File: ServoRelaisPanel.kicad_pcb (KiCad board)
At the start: 2 copper layers, 77.5 x 99.9 mm, 160 parts, among them J1 Conn_01x03_Female, J2 ISCP, J3 Conn_01x02_Female, J4 Conn_01x03_Female, U1 L78L05_SOT89, U2 PIC10F320-IP, U3 ASSR-1611

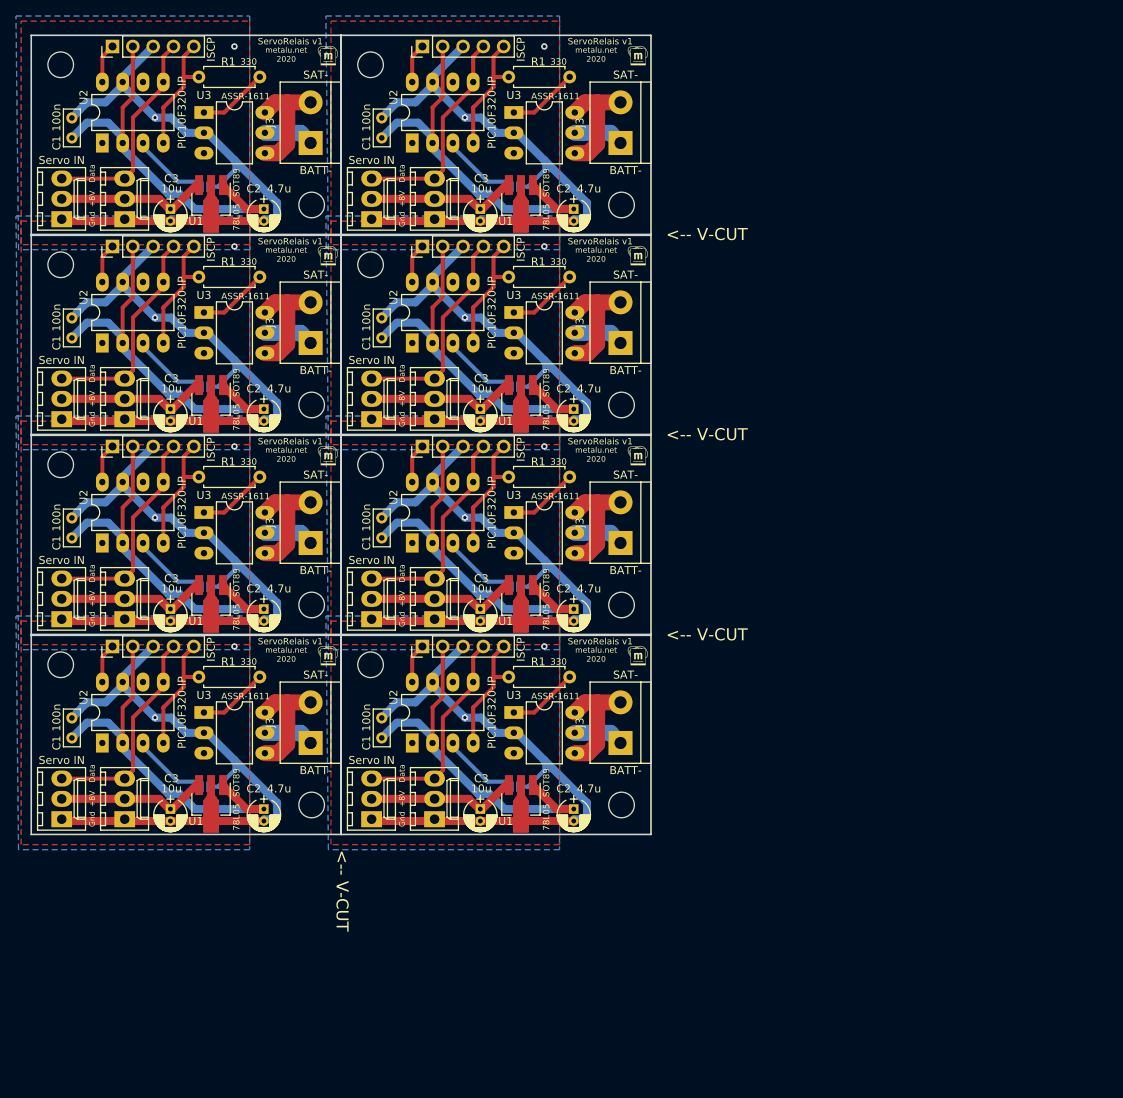
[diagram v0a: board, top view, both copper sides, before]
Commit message: finish PCB, using ASSR-1611 as a 5A circuit breaker.
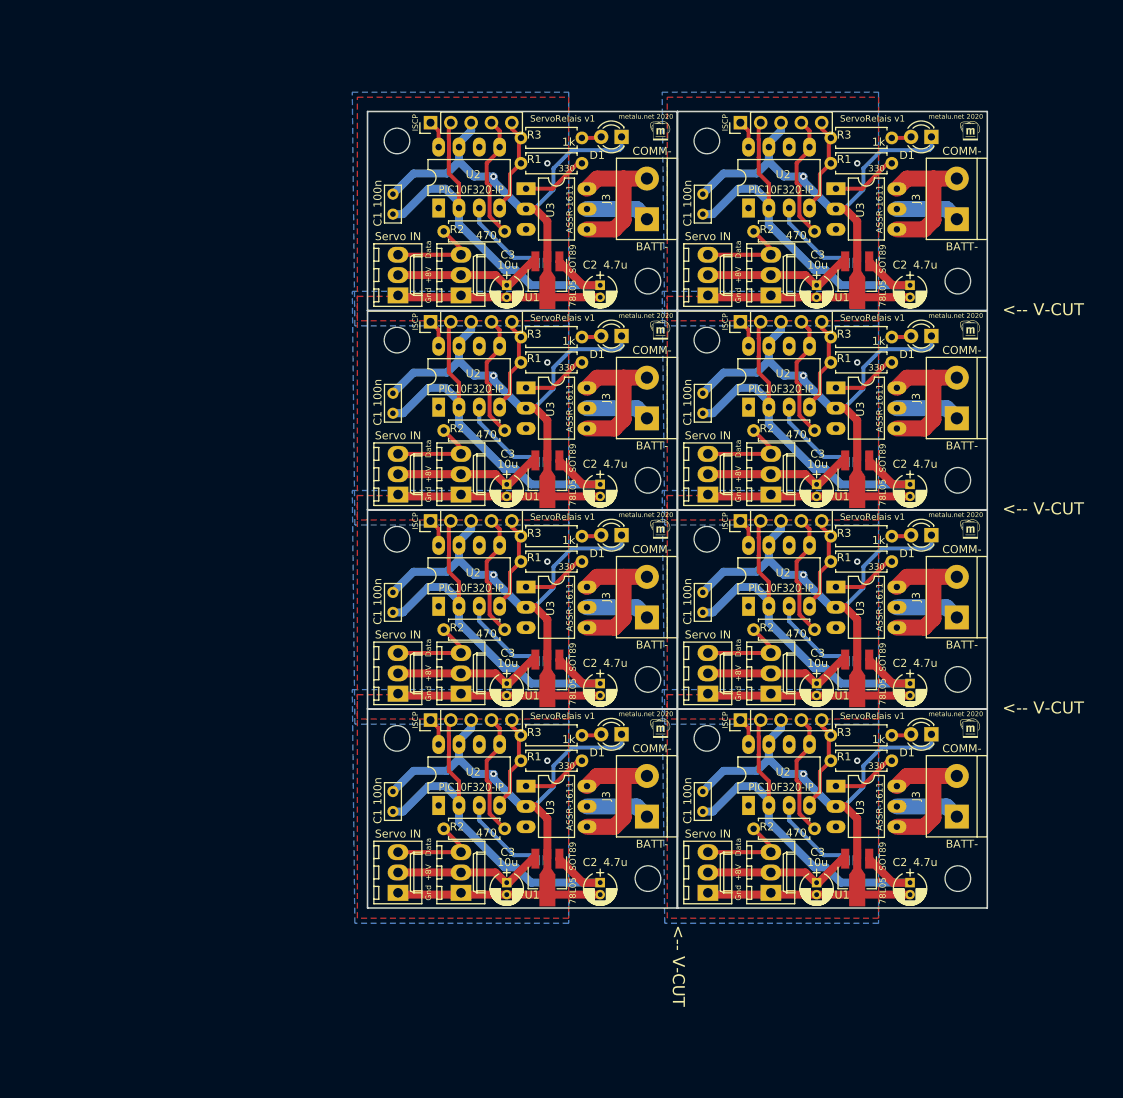
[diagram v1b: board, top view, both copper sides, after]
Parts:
- removed the ? at (110.0, 97.0)
- removed the ? at (71.2, 97.0)
- removed the ? at (110.0, 72.0)
- removed the ? at (71.2, 72.0)
- removed the ? at (110.0, 47.0)
- removed the ? at (108.7, 122.0)
- removed the ? at (70.0, 122.0)
- removed the ? at (108.7, 97.0)
- removed the ? at (70.0, 97.0)
- removed the ? at (108.7, 72.0)
- removed the ? at (70.0, 72.0)
- removed the ? at (108.7, 47.0)
- removed the ? at (108.7, 123.3)
- removed the ? at (70.0, 123.3)
- removed the ? at (108.7, 98.3)
- removed the ? at (70.0, 98.3)
- removed the ? at (108.7, 73.3)
- removed the ? at (70.0, 73.3)
- removed the ? at (108.7, 48.3)
- removed the ? at (71.2, 58.4)
- removed the ? at (110.0, 108.4)
- removed the ? at (70.0, 47.0)
- removed the ? at (71.2, 47.0)
- removed the ? at (70.0, 48.3)
- removed the ? at (71.2, 108.4)
- removed the ? at (110.0, 83.4)
- removed the ? at (71.2, 83.4)
- removed the ? at (110.0, 58.4)
- removed the ? at (110.0, 122.0)
- removed the ? at (71.2, 122.0)
- removed the C1 at (100.5, 118.2)
- removed the C1 at (61.7, 118.2)
- removed the C1 at (100.5, 93.2)
- removed the C1 at (61.7, 93.2)
- removed the C1 at (100.5, 68.2)
- removed the C1 at (61.7, 68.2)
- removed the C1 at (100.5, 43.2)
- removed the C2 at (124.5, 127.1)
- removed the C2 at (85.7, 127.1)
- removed the C2 at (124.5, 102.1)
- removed the C2 at (85.7, 102.1)
- removed the C2 at (124.5, 77.1)
- removed the C2 at (85.7, 77.1)
- removed the C2 at (124.5, 52.1)
- removed the C3 at (112.8, 127.1)
- removed the C3 at (74.0, 127.1)
- removed the C3 at (112.8, 102.1)
- removed the C3 at (74.0, 102.1)
- removed the C3 at (112.8, 77.1)
- removed the C3 at (74.0, 77.1)
- removed the C3 at (112.8, 52.1)
- removed the G*** at (128.4, 107.8)
- removed the G*** at (132.5, 82.9)
- removed the G*** at (93.7, 82.9)
- removed the G*** at (132.5, 57.9)
- removed the G*** at (93.7, 57.9)
- removed the G*** at (132.5, 32.9)
- removed the G*** at (89.7, 107.8)
- removed the G*** at (128.4, 82.8)
- removed the G*** at (89.7, 82.8)
- removed the G*** at (128.4, 57.8)
- removed the G*** at (89.7, 57.8)
- removed the G*** at (128.4, 32.8)
- removed the G*** at (132.5, 107.9)
- removed the G*** at (93.7, 107.9)
- removed the H1 at (99.1, 109.0)
- removed the H1 at (60.3, 109.0)
- removed the H1 at (99.1, 84.0)
- removed the H1 at (60.3, 84.0)
- removed the H1 at (99.1, 59.0)
- removed the H1 at (60.3, 59.0)
- removed the H1 at (99.1, 34.0)
- removed the H2 at (130.4, 126.6)
- removed the H2 at (91.7, 126.6)
- removed the H2 at (130.4, 101.6)
- removed the H2 at (91.7, 101.6)
- removed the H2 at (130.4, 76.6)
- removed the H2 at (91.7, 76.6)
- removed the H2 at (130.4, 51.6)
- removed the J1 at (99.2, 128.3)
- removed the J1 at (60.5, 128.3)
- removed the J1 at (99.2, 103.3)
- removed the J1 at (60.5, 103.3)
- removed the J1 at (99.2, 78.3)
- removed the J1 at (60.5, 78.3)
- removed the J1 at (99.2, 53.3)
- removed the J2 at (105.5, 106.8)
- removed the J2 at (66.8, 106.8)
- removed the J2 at (105.5, 81.8)
- removed the J2 at (66.8, 81.8)
- removed the J2 at (105.5, 56.8)
- removed the J2 at (66.8, 56.8)
- removed the J2 at (105.5, 31.8)
- removed the J3 at (130.3, 118.8)
- removed the J3 at (91.6, 118.8)
- removed the J3 at (130.3, 93.8)
- removed the J3 at (91.6, 93.8)
- removed the J3 at (130.3, 68.8)
- removed the J3 at (91.6, 68.8)
- removed the J3 at (130.3, 43.8)
- removed the J4 at (107.1, 128.3)
- removed the J4 at (68.3, 128.3)
- removed the J4 at (107.1, 103.3)
- removed the J4 at (68.3, 103.3)
- removed the J4 at (107.1, 78.3)
- removed the J4 at (68.3, 78.3)
- removed the J4 at (107.1, 53.3)
- removed the JP1 at (117.1, 124.3)
- removed the JP1 at (78.4, 124.3)
- removed the JP1 at (117.1, 99.3)
- removed the JP1 at (78.4, 99.3)
- removed the JP1 at (117.1, 74.3)
- removed the JP1 at (78.4, 74.3)
- removed the JP1 at (117.1, 49.3)
- removed the R1 at (124.0, 110.6)
- removed the R1 at (85.2, 110.6)
- removed the R1 at (124.0, 85.6)
- removed the R1 at (85.2, 85.6)
- removed the R1 at (124.0, 60.6)
- removed the R1 at (85.2, 60.6)
- removed the R1 at (124.0, 35.6)
- removed the U1 at (117.9, 126.1)
- removed the U1 at (79.1, 126.1)
- removed the U1 at (117.9, 101.1)
- removed the U1 at (79.1, 101.1)
- removed the U1 at (117.9, 76.1)
- removed the U1 at (79.1, 76.1)
- removed the U1 at (117.9, 51.1)
- removed the U2 at (104.3, 118.8)
- removed the U2 at (65.5, 118.8)
- removed the U2 at (104.3, 93.8)
- removed the U2 at (65.5, 93.8)
- removed the U2 at (104.3, 68.8)
- removed the U2 at (65.5, 68.8)
- removed the U2 at (104.3, 43.8)
- removed the U3 at (117.0, 115.0)
- removed the U3 at (78.2, 115.0)
- removed the U3 at (117.0, 90.0)
- removed the U3 at (78.2, 90.0)
- removed the U3 at (117.0, 65.0)
- removed the U3 at (78.2, 65.0)
- removed the U3 at (117.0, 40.0)
- added ?: , , F.Cu at (152.0, 131.2)
- added ?: , , F.Cu at (150.7, 107.6)
- added ?: , , F.Cu at (112.0, 107.6)
- added ?: , , F.Cu at (150.7, 82.7)
- added ?: , , F.Cu at (112.0, 82.7)
- added ?: , , F.Cu at (150.7, 57.8)
- added ? (x3): , , F.Cu at (152.0, 142.6)
- added ? (x2): , , F.Cu at (113.3, 142.6)
- added ?: , , F.Cu at (152.0, 117.7)
- added ?: , , F.Cu at (113.3, 117.7)
- added ?: , , F.Cu at (152.0, 92.8)
- added ?: , , F.Cu at (113.3, 131.2)
- added ?: , , F.Cu at (113.3, 92.8)
- added ?: , , F.Cu at (152.0, 67.9)
- added ?: , , F.Cu at (150.7, 131.2)
- added ?: , , F.Cu at (112.0, 131.2)
- added ?: , , F.Cu at (150.7, 106.3)
- added ?: , , F.Cu at (112.0, 106.3)
- added ?: , , F.Cu at (150.7, 81.4)
- added ?: , , F.Cu at (112.0, 81.4)
- added ?: , , F.Cu at (150.7, 56.5)
- added ?: , , F.Cu at (152.0, 106.3)
- added ?: , , F.Cu at (113.3, 67.9)
- added ?: , , F.Cu at (112.0, 56.5)
- added ?: , , F.Cu at (113.3, 56.5)
- added ?: , , F.Cu at (112.0, 57.8)
- added ?: , , F.Cu at (113.3, 106.3)
- added ?: , , F.Cu at (152.0, 81.4)
- added ?: , , F.Cu at (113.3, 81.4)
- added ?: , , F.Cu at (152.0, 56.5)
- added ?: , , F.Cu at (150.7, 132.5)
- added ?: , , F.Cu at (112.0, 132.5)
- added C1: 100n, Capacitors_ThroughHole:C_Rect_L4.6mm_W2.0mm_P2.50mm_MKS02_FKP02, F.Cu at (140.6, 127.4)
- added C1: 100n, Capacitors_ThroughHole:C_Rect_L4.6mm_W2.0mm_P2.50mm_MKS02_FKP02, F.Cu at (101.9, 127.4)
- added C1: 100n, Capacitors_ThroughHole:C_Rect_L4.6mm_W2.0mm_P2.50mm_MKS02_FKP02, F.Cu at (140.6, 102.5)
- added C1: 100n, Capacitors_ThroughHole:C_Rect_L4.6mm_W2.0mm_P2.50mm_MKS02_FKP02, F.Cu at (101.9, 102.5)
- added C1: 100n, Capacitors_ThroughHole:C_Rect_L4.6mm_W2.0mm_P2.50mm_MKS02_FKP02, F.Cu at (140.6, 77.6)
- added C1: 100n, Capacitors_ThroughHole:C_Rect_L4.6mm_W2.0mm_P2.50mm_MKS02_FKP02, F.Cu at (101.9, 77.6)
- added C1: 100n, Capacitors_ThroughHole:C_Rect_L4.6mm_W2.0mm_P2.50mm_MKS02_FKP02, F.Cu at (140.6, 52.7)
- added C2: 4.7u, Capacitors_ThroughHole:CP_Radial_D4.0mm_P1.50mm, F.Cu at (166.5, 136.3)
- added C2: 4.7u, Capacitors_ThroughHole:CP_Radial_D4.0mm_P1.50mm, F.Cu at (127.8, 136.3)
- added C2: 4.7u, Capacitors_ThroughHole:CP_Radial_D4.0mm_P1.50mm, F.Cu at (166.5, 111.4)
- added C2: 4.7u, Capacitors_ThroughHole:CP_Radial_D4.0mm_P1.50mm, F.Cu at (127.8, 111.4)
- added C2: 4.7u, Capacitors_ThroughHole:CP_Radial_D4.0mm_P1.50mm, F.Cu at (166.5, 86.5)
- added C2: 4.7u, Capacitors_ThroughHole:CP_Radial_D4.0mm_P1.50mm, F.Cu at (127.8, 86.5)
- added C2: 4.7u, Capacitors_ThroughHole:CP_Radial_D4.0mm_P1.50mm, F.Cu at (166.5, 61.6)
- added C3: 10u, Capacitors_ThroughHole:CP_Radial_D4.0mm_P1.50mm, F.Cu at (154.8, 136.3)
- added C3: 10u, Capacitors_ThroughHole:CP_Radial_D4.0mm_P1.50mm, F.Cu at (116.1, 136.3)
- added C3: 10u, Capacitors_ThroughHole:CP_Radial_D4.0mm_P1.50mm, F.Cu at (154.8, 111.4)
- added C3: 10u, Capacitors_ThroughHole:CP_Radial_D4.0mm_P1.50mm, F.Cu at (116.1, 111.4)
- added C3: 10u, Capacitors_ThroughHole:CP_Radial_D4.0mm_P1.50mm, F.Cu at (154.8, 86.5)
- added C3: 10u, Capacitors_ThroughHole:CP_Radial_D4.0mm_P1.50mm, F.Cu at (116.1, 86.5)
- added C3: 10u, Capacitors_ThroughHole:CP_Radial_D4.0mm_P1.50mm, F.Cu at (154.8, 61.6)
- added D1: LED, LEDs:LED_D3.0mm, F.Cu at (169.2, 117.7)
- added D1: LED, LEDs:LED_D3.0mm, F.Cu at (130.4, 117.7)
- added D1: LED, LEDs:LED_D3.0mm, F.Cu at (169.2, 92.8)
- added D1: LED, LEDs:LED_D3.0mm, F.Cu at (130.4, 92.8)
- added D1: LED, LEDs:LED_D3.0mm, F.Cu at (169.2, 67.9)
- added D1: LED, LEDs:LED_D3.0mm, F.Cu at (130.4, 67.9)
- added D1: LED, LEDs:LED_D3.0mm, F.Cu at (169.2, 43.1)
- added D1: LED, LEDs:LED_D3.0mm, F.Cu at (130.4, 43.1)
- added G***: LOGO, metalunet:metalunet, B.Cu at (166.9, 132.3)
- added G***: LOGO, metalunet:metalunet-mini, F.Cu at (174.0, 92.1)
- added G***: LOGO, metalunet:metalunet-mini, F.Cu at (135.3, 92.1)
- added G***: LOGO, metalunet:metalunet-mini, F.Cu at (174.0, 67.2)
- added G***: LOGO, metalunet:metalunet-mini, F.Cu at (135.3, 67.2)
- added G***: LOGO, metalunet:metalunet-mini, F.Cu at (174.0, 42.3)
- added G***: LOGO, metalunet:metalunet, B.Cu at (128.1, 132.3)
- added G***: LOGO, metalunet:metalunet, B.Cu at (166.9, 107.4)
- added G***: LOGO, metalunet:metalunet, B.Cu at (128.1, 107.4)
- added G***: LOGO, metalunet:metalunet, B.Cu at (166.9, 82.5)
- added G***: LOGO, metalunet:metalunet, B.Cu at (128.1, 82.5)
- added G***: LOGO, metalunet:metalunet, B.Cu at (166.9, 57.7)
- added G***: LOGO, metalunet:metalunet-mini, F.Cu at (174.0, 117.0)
- added G***: LOGO, metalunet:metalunet-mini, F.Cu at (135.3, 117.0)
- added H1: MountingHole, Mounting_Holes:MountingHole_3.2mm_M3, F.Cu at (141.1, 118.2)
- added H1: MountingHole, Mounting_Holes:MountingHole_3.2mm_M3, F.Cu at (102.4, 118.2)
- added H1: MountingHole, Mounting_Holes:MountingHole_3.2mm_M3, F.Cu at (141.1, 93.3)
- added H1: MountingHole, Mounting_Holes:MountingHole_3.2mm_M3, F.Cu at (102.4, 93.3)
- added H1: MountingHole, Mounting_Holes:MountingHole_3.2mm_M3, F.Cu at (141.1, 68.5)
- added H1: MountingHole, Mounting_Holes:MountingHole_3.2mm_M3, F.Cu at (102.4, 68.5)
- added H1: MountingHole, Mounting_Holes:MountingHole_3.2mm_M3, F.Cu at (141.1, 43.6)
- added H2: MountingHole, Mounting_Holes:MountingHole_3.2mm_M3, F.Cu at (172.5, 135.8)
- added H2: MountingHole, Mounting_Holes:MountingHole_3.2mm_M3, F.Cu at (133.7, 135.8)
- added H2: MountingHole, Mounting_Holes:MountingHole_3.2mm_M3, F.Cu at (172.5, 110.9)
- added H2: MountingHole, Mounting_Holes:MountingHole_3.2mm_M3, F.Cu at (133.7, 110.9)
- added H2: MountingHole, Mounting_Holes:MountingHole_3.2mm_M3, F.Cu at (172.5, 86.0)
- added H2: MountingHole, Mounting_Holes:MountingHole_3.2mm_M3, F.Cu at (133.7, 86.0)
- added H2: MountingHole, Mounting_Holes:MountingHole_3.2mm_M3, F.Cu at (172.5, 61.1)
- added J1: Conn_01x03_Female, Connectors_Molex:Molex_KK-6410-03_03x2.54mm_Straight, F.Cu at (141.2, 137.5)
- added J1: Conn_01x03_Female, Connectors_Molex:Molex_KK-6410-03_03x2.54mm_Straight, F.Cu at (102.5, 137.5)
- added J1: Conn_01x03_Female, Connectors_Molex:Molex_KK-6410-03_03x2.54mm_Straight, F.Cu at (141.2, 112.6)
- added J1: Conn_01x03_Female, Connectors_Molex:Molex_KK-6410-03_03x2.54mm_Straight, F.Cu at (102.5, 112.6)
- added J1: Conn_01x03_Female, Connectors_Molex:Molex_KK-6410-03_03x2.54mm_Straight, F.Cu at (141.2, 87.8)
- added J1: Conn_01x03_Female, Connectors_Molex:Molex_KK-6410-03_03x2.54mm_Straight, F.Cu at (102.5, 87.8)
- added J1: Conn_01x03_Female, Connectors_Molex:Molex_KK-6410-03_03x2.54mm_Straight, F.Cu at (141.2, 62.9)
- added J2: ISCP, Pin_Headers:Pin_Header_Straight_1x05_Pitch2.54mm, F.Cu at (145.3, 116.0)
- added J2: ISCP, Pin_Headers:Pin_Header_Straight_1x05_Pitch2.54mm, F.Cu at (106.6, 116.0)
- added J2: ISCP, Pin_Headers:Pin_Header_Straight_1x05_Pitch2.54mm, F.Cu at (145.3, 91.1)
- added J2: ISCP, Pin_Headers:Pin_Header_Straight_1x05_Pitch2.54mm, F.Cu at (106.6, 91.1)
- added J2: ISCP, Pin_Headers:Pin_Header_Straight_1x05_Pitch2.54mm, F.Cu at (145.3, 66.2)
- added J2: ISCP, Pin_Headers:Pin_Header_Straight_1x05_Pitch2.54mm, F.Cu at (106.6, 66.2)
- added J2: ISCP, Pin_Headers:Pin_Header_Straight_1x05_Pitch2.54mm, F.Cu at (145.3, 41.3)
- added J3: Conn_01x02_Female, Terminal_Blocks:TerminalBlock_bornier-2_P5.08mm, F.Cu at (172.3, 128.0)
- added J3: Conn_01x02_Female, Terminal_Blocks:TerminalBlock_bornier-2_P5.08mm, F.Cu at (133.6, 128.0)
- added J3: Conn_01x02_Female, Terminal_Blocks:TerminalBlock_bornier-2_P5.08mm, F.Cu at (172.3, 103.1)
- added J3: Conn_01x02_Female, Terminal_Blocks:TerminalBlock_bornier-2_P5.08mm, F.Cu at (133.6, 103.1)
- added J3: Conn_01x02_Female, Terminal_Blocks:TerminalBlock_bornier-2_P5.08mm, F.Cu at (172.3, 78.2)
- added J3: Conn_01x02_Female, Terminal_Blocks:TerminalBlock_bornier-2_P5.08mm, F.Cu at (133.6, 78.2)
- added J3: Conn_01x02_Female, Terminal_Blocks:TerminalBlock_bornier-2_P5.08mm, F.Cu at (172.3, 53.3)
- added J4: Conn_01x03_Female, Connectors_Molex:Molex_KK-6410-03_03x2.54mm_Straight, F.Cu at (149.1, 137.5)
- added J4: Conn_01x03_Female, Connectors_Molex:Molex_KK-6410-03_03x2.54mm_Straight, F.Cu at (110.4, 137.5)
- added J4: Conn_01x03_Female, Connectors_Molex:Molex_KK-6410-03_03x2.54mm_Straight, F.Cu at (149.1, 112.6)
- added J4: Conn_01x03_Female, Connectors_Molex:Molex_KK-6410-03_03x2.54mm_Straight, F.Cu at (110.4, 112.6)
- added J4: Conn_01x03_Female, Connectors_Molex:Molex_KK-6410-03_03x2.54mm_Straight, F.Cu at (149.1, 87.8)
- added J4: Conn_01x03_Female, Connectors_Molex:Molex_KK-6410-03_03x2.54mm_Straight, F.Cu at (110.4, 87.8)
- added J4: Conn_01x03_Female, Connectors_Molex:Molex_KK-6410-03_03x2.54mm_Straight, F.Cu at (149.1, 62.9)
- added JP1: Config, Connect:GS2, B.Cu at (159.1, 133.5)
- added JP1: Config, Connect:GS2, B.Cu at (120.4, 133.5)
- added JP1: Config, Connect:GS2, B.Cu at (159.1, 108.6)
- added JP1: Config, Connect:GS2, B.Cu at (120.4, 108.6)
- added JP1: Config, Connect:GS2, B.Cu at (159.1, 83.7)
- added JP1: Config, Connect:GS2, B.Cu at (120.4, 83.7)
- added JP1: Config, Connect:GS2, B.Cu at (159.1, 58.8)
- added R1: 330, Resistors_ThroughHole:R_Axial_DIN0207_L6.3mm_D2.5mm_P7.62mm_Horizontal, F.Cu at (164.2, 121.0)
- added R1: 330, Resistors_ThroughHole:R_Axial_DIN0207_L6.3mm_D2.5mm_P7.62mm_Horizontal, F.Cu at (125.5, 121.0)
- added R1: 330, Resistors_ThroughHole:R_Axial_DIN0207_L6.3mm_D2.5mm_P7.62mm_Horizontal, F.Cu at (164.2, 96.1)
- added R1: 330, Resistors_ThroughHole:R_Axial_DIN0207_L6.3mm_D2.5mm_P7.62mm_Horizontal, F.Cu at (125.5, 96.1)
- added R1: 330, Resistors_ThroughHole:R_Axial_DIN0207_L6.3mm_D2.5mm_P7.62mm_Horizontal, F.Cu at (164.2, 71.2)
- added R1: 330, Resistors_ThroughHole:R_Axial_DIN0207_L6.3mm_D2.5mm_P7.62mm_Horizontal, F.Cu at (125.5, 71.2)
- added R1: 330, Resistors_ThroughHole:R_Axial_DIN0207_L6.3mm_D2.5mm_P7.62mm_Horizontal, F.Cu at (164.2, 46.4)
- added R2: 470, Resistors_ThroughHole:R_Axial_DIN0207_L6.3mm_D2.5mm_P7.62mm_Horizontal, F.Cu at (154.6, 129.5)
- added R2: 470, Resistors_ThroughHole:R_Axial_DIN0207_L6.3mm_D2.5mm_P7.62mm_Horizontal, F.Cu at (115.8, 129.5)
- added R2: 470, Resistors_ThroughHole:R_Axial_DIN0207_L6.3mm_D2.5mm_P7.62mm_Horizontal, F.Cu at (154.6, 104.6)
- added R2: 470, Resistors_ThroughHole:R_Axial_DIN0207_L6.3mm_D2.5mm_P7.62mm_Horizontal, F.Cu at (115.8, 104.6)
- added R2: 470, Resistors_ThroughHole:R_Axial_DIN0207_L6.3mm_D2.5mm_P7.62mm_Horizontal, F.Cu at (154.6, 79.8)
- added R2: 470, Resistors_ThroughHole:R_Axial_DIN0207_L6.3mm_D2.5mm_P7.62mm_Horizontal, F.Cu at (115.8, 79.8)
- added R2: 470, Resistors_ThroughHole:R_Axial_DIN0207_L6.3mm_D2.5mm_P7.62mm_Horizontal, F.Cu at (154.6, 54.9)
- added R2: 470, Resistors_ThroughHole:R_Axial_DIN0207_L6.3mm_D2.5mm_P7.62mm_Horizontal, F.Cu at (115.8, 54.9)
- added R3: 1k, Resistors_ThroughHole:R_Axial_DIN0207_L6.3mm_D2.5mm_P7.62mm_Horizontal, F.Cu at (164.2, 117.9)
- added R3: 1k, Resistors_ThroughHole:R_Axial_DIN0207_L6.3mm_D2.5mm_P7.62mm_Horizontal, F.Cu at (125.5, 117.9)
- added R3: 1k, Resistors_ThroughHole:R_Axial_DIN0207_L6.3mm_D2.5mm_P7.62mm_Horizontal, F.Cu at (164.2, 93.0)
- added R3: 1k, Resistors_ThroughHole:R_Axial_DIN0207_L6.3mm_D2.5mm_P7.62mm_Horizontal, F.Cu at (125.5, 93.0)
- added R3: 1k, Resistors_ThroughHole:R_Axial_DIN0207_L6.3mm_D2.5mm_P7.62mm_Horizontal, F.Cu at (164.2, 68.1)
- added R3: 1k, Resistors_ThroughHole:R_Axial_DIN0207_L6.3mm_D2.5mm_P7.62mm_Horizontal, F.Cu at (125.5, 68.1)
- added R3: 1k, Resistors_ThroughHole:R_Axial_DIN0207_L6.3mm_D2.5mm_P7.62mm_Horizontal, F.Cu at (164.2, 43.2)
- added R3: 1k, Resistors_ThroughHole:R_Axial_DIN0207_L6.3mm_D2.5mm_P7.62mm_Horizontal, F.Cu at (125.5, 43.2)
- added U1: L78L05_SOT89, TO_SOT_Packages_SMD:SOT-89-3_Handsoldering, F.Cu at (159.9, 135.3)
- added U1: L78L05_SOT89, TO_SOT_Packages_SMD:SOT-89-3_Handsoldering, F.Cu at (121.2, 135.3)
- added U1: L78L05_SOT89, TO_SOT_Packages_SMD:SOT-89-3_Handsoldering, F.Cu at (159.9, 110.4)
- added U1: L78L05_SOT89, TO_SOT_Packages_SMD:SOT-89-3_Handsoldering, F.Cu at (121.2, 110.4)
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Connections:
- J1 pad 3: /PGD -> Net-(J1-Pad3)
- J4 pad 3: /PGD -> Net-(J1-Pad3)
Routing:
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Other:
- board size 77.5 x 99.9 mm -> 77.5 x 99.6 mm
- board text added: "COMM-"
- board text removed: "SAT-"

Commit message: use a 3v->9V dc-dc converter. version 1.3
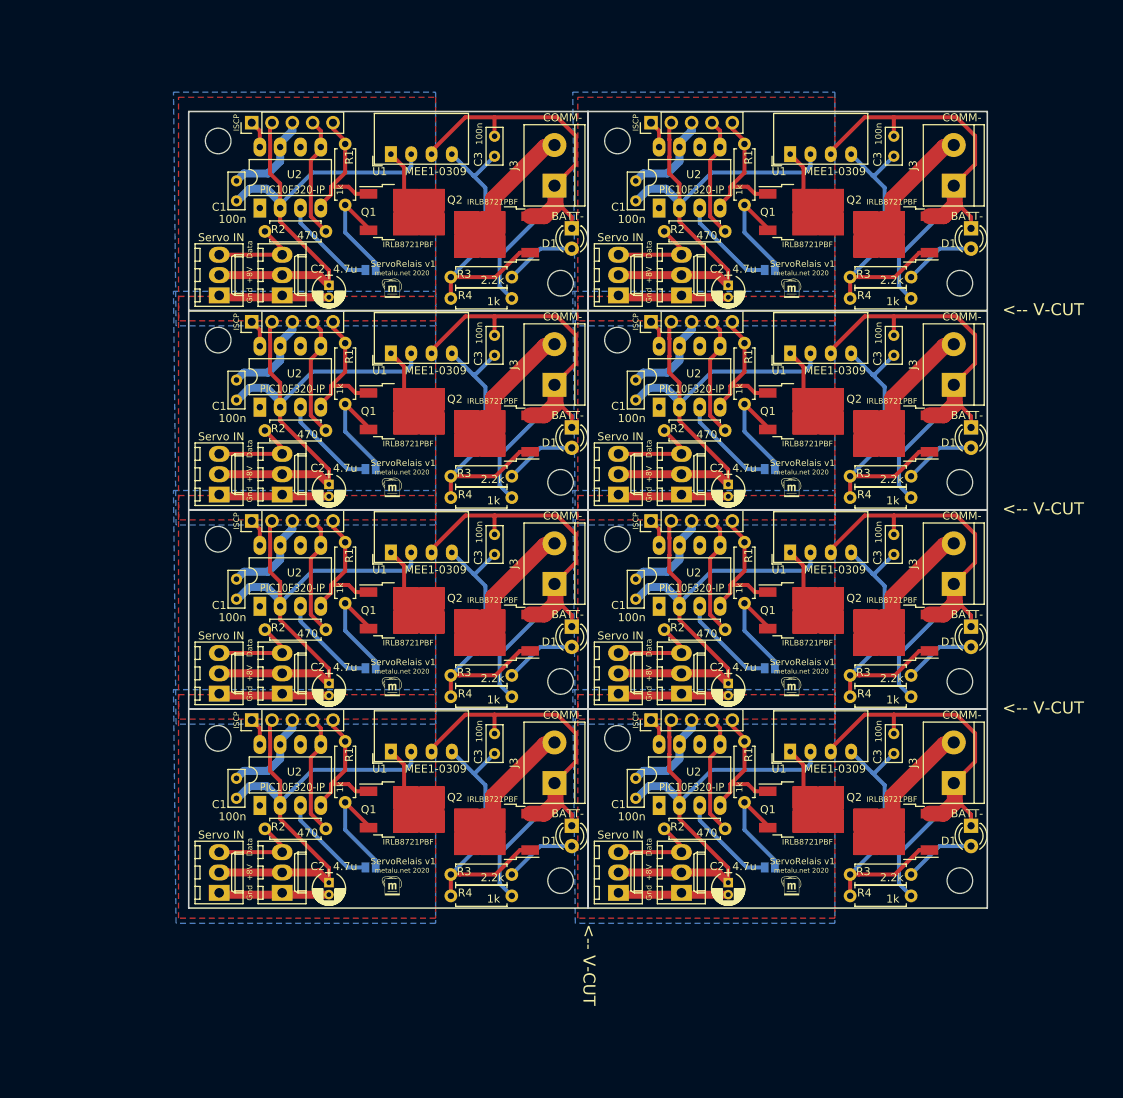
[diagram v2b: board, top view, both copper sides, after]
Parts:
- removed the ? at (152.0, 131.2)
- removed the ? at (150.7, 107.6)
- removed the ? at (112.0, 107.6)
- removed the ? at (150.7, 82.7)
- removed the ? at (112.0, 82.7)
- removed the ? at (150.7, 57.8)
- removed the ? at (152.0, 142.6) (x3)
- removed the ? at (113.3, 142.6) (x2)
- removed the ? at (152.0, 117.7)
- removed the ? at (113.3, 117.7)
- removed the ? at (152.0, 92.8)
- removed the ? at (113.3, 131.2)
- removed the ? at (113.3, 92.8)
- removed the ? at (152.0, 67.9)
- removed the ? at (150.7, 131.2)
- removed the ? at (112.0, 131.2)
- removed the ? at (150.7, 106.3)
- removed the ? at (112.0, 106.3)
- removed the ? at (150.7, 81.4)
- removed the ? at (112.0, 81.4)
- removed the ? at (150.7, 56.5)
- removed the ? at (152.0, 106.3)
- removed the ? at (113.3, 67.9)
- removed the ? at (112.0, 56.5)
- removed the ? at (113.3, 56.5)
- removed the ? at (112.0, 57.8)
- removed the ? at (113.3, 106.3)
- removed the ? at (152.0, 81.4)
- removed the ? at (113.3, 81.4)
- removed the ? at (152.0, 56.5)
- removed the ? at (150.7, 132.5)
- removed the ? at (112.0, 132.5)
- removed the C1 at (140.6, 127.4)
- removed the C1 at (101.9, 127.4)
- removed the C1 at (140.6, 102.5)
- removed the C1 at (101.9, 102.5)
- removed the C1 at (140.6, 77.6)
- removed the C1 at (101.9, 77.6)
- removed the C1 at (140.6, 52.7)
- removed the C1 at (101.9, 52.7)
- removed the C2 at (166.5, 136.3)
- removed the C2 at (127.8, 136.3)
- removed the C2 at (166.5, 111.4)
- removed the C2 at (127.8, 111.4)
- removed the C2 at (166.5, 86.5)
- removed the C2 at (127.8, 86.5)
- removed the C2 at (166.5, 61.6)
- removed the C3 at (154.8, 136.3)
- removed the C3 at (116.1, 136.3)
- removed the C3 at (154.8, 111.4)
- removed the C3 at (116.1, 111.4)
- removed the C3 at (154.8, 86.5)
- removed the C3 at (116.1, 86.5)
- removed the C3 at (154.8, 61.6)
- removed the C3 at (116.1, 61.6)
- removed the D1 at (169.2, 117.7)
- removed the D1 at (130.4, 117.7)
- removed the D1 at (169.2, 92.8)
- removed the D1 at (130.4, 92.8)
- removed the D1 at (169.2, 67.9)
- removed the D1 at (130.4, 67.9)
- removed the D1 at (169.2, 43.1)
- removed the D1 at (130.4, 43.1)
- removed the G*** at (166.9, 132.3)
- removed the G*** at (174.0, 92.1)
- removed the G*** at (135.3, 92.1)
- removed the G*** at (174.0, 67.2)
- removed the G*** at (135.3, 67.2)
- removed the G*** at (174.0, 42.3)
- removed the G*** at (128.1, 57.7)
- removed the G*** at (135.3, 42.3)
- removed the G*** at (128.1, 132.3)
- removed the G*** at (166.9, 107.4)
- removed the G*** at (128.1, 107.4)
- removed the G*** at (166.9, 82.5)
- removed the G*** at (128.1, 82.5)
- removed the G*** at (166.9, 57.7)
- removed the G*** at (174.0, 117.0)
- removed the G*** at (135.3, 117.0)
- removed the H1 at (141.1, 118.2)
- removed the H1 at (102.4, 118.2)
- removed the H1 at (141.1, 93.3)
- removed the H1 at (102.4, 93.3)
- removed the H1 at (141.1, 68.5)
- removed the H1 at (102.4, 68.5)
- removed the H1 at (141.1, 43.6)
- removed the H2 at (172.5, 135.8)
- removed the H2 at (133.7, 135.8)
- removed the H2 at (172.5, 110.9)
- removed the H2 at (133.7, 110.9)
- removed the H2 at (172.5, 86.0)
- removed the H2 at (133.7, 86.0)
- removed the H2 at (172.5, 61.1)
- removed the J1 at (141.2, 137.5)
- removed the J1 at (102.5, 137.5)
- removed the J1 at (141.2, 112.6)
- removed the J1 at (102.5, 112.6)
- removed the J1 at (141.2, 87.8)
- removed the J1 at (102.5, 87.8)
- removed the J1 at (141.2, 62.9)
- removed the J2 at (145.3, 116.0)
- removed the J2 at (106.6, 116.0)
- removed the J2 at (145.3, 91.1)
- removed the J2 at (106.6, 91.1)
- removed the J2 at (145.3, 66.2)
- removed the J2 at (106.6, 66.2)
- removed the J2 at (145.3, 41.3)
- removed the J3 at (172.3, 128.0)
- removed the J3 at (133.6, 128.0)
- removed the J3 at (172.3, 103.1)
- removed the J3 at (133.6, 103.1)
- removed the J3 at (172.3, 78.2)
- removed the J3 at (133.6, 78.2)
- removed the J3 at (172.3, 53.3)
- removed the J4 at (149.1, 137.5)
- removed the J4 at (110.4, 137.5)
- removed the J4 at (149.1, 112.6)
- removed the J4 at (110.4, 112.6)
- removed the J4 at (149.1, 87.8)
- removed the J4 at (110.4, 87.8)
- removed the J4 at (149.1, 62.9)
- removed the JP1 at (159.1, 133.5)
- removed the JP1 at (120.4, 133.5)
- removed the JP1 at (159.1, 108.6)
- removed the JP1 at (120.4, 108.6)
- removed the JP1 at (159.1, 83.7)
- removed the JP1 at (120.4, 83.7)
- removed the JP1 at (159.1, 58.8)
- removed the R1 at (164.2, 121.0)
- removed the R1 at (125.5, 121.0)
- removed the R1 at (164.2, 96.1)
- removed the R1 at (125.5, 96.1)
- removed the R1 at (164.2, 71.2)
- removed the R1 at (125.5, 71.2)
- removed the R1 at (164.2, 46.4)
- removed the R2 at (154.6, 129.5)
- removed the R2 at (115.8, 129.5)
- removed the R2 at (154.6, 104.6)
- removed the R2 at (115.8, 104.6)
- removed the R2 at (154.6, 79.8)
- removed the R2 at (115.8, 79.8)
- removed the R2 at (154.6, 54.9)
- removed the R2 at (115.8, 54.9)
- removed the R3 at (164.2, 117.9)
- removed the R3 at (125.5, 117.9)
- removed the R3 at (164.2, 93.0)
- removed the R3 at (125.5, 93.0)
- removed the R3 at (164.2, 68.1)
- removed the R3 at (125.5, 68.1)
- removed the R3 at (164.2, 43.2)
- removed the U1 at (159.9, 135.3)
- removed the U1 at (121.2, 135.3)
- removed the U1 at (159.9, 110.4)
- removed the U1 at (121.2, 110.4)
- removed the U1 at (159.9, 85.5)
- removed the U1 at (121.2, 85.5)
- removed the U1 at (159.9, 60.6)
- removed the U1 at (121.2, 60.6)
- removed the U2 at (146.3, 126.6)
- removed the U2 at (107.6, 126.6)
- removed the U2 at (146.3, 101.7)
- removed the U2 at (107.6, 101.7)
- removed the U2 at (146.3, 76.8)
- removed the U2 at (107.6, 76.8)
- removed the U2 at (146.3, 51.9)
- removed the U2 at (107.6, 51.9)
- removed U3 (x8): ASSR-1611, Housings_DIP:DIP-6_W7.62mm_LongPads
- added ?: , , F.Cu at (140.8, 142.6)
- added ?: , , F.Cu at (140.8, 106.3)
- added ?: , , F.Cu at (90.9, 106.3)
- added ?: , , F.Cu at (140.8, 81.4)
- added ?: , , F.Cu at (90.9, 81.4)
- added ?: , , F.Cu at (140.8, 56.5)
- added ?: , , F.Cu at (139.6, 131.2)
- added ?: , , F.Cu at (89.7, 131.2)
- added ?: , , F.Cu at (139.6, 106.3)
- added ?: , , F.Cu at (89.7, 106.3)
- added ?: , , F.Cu at (139.6, 81.4)
- added ?: , , F.Cu at (90.9, 142.6)
- added ?: , , F.Cu at (89.7, 81.4)
- added ?: , , F.Cu at (139.6, 56.5)
- added ?: , , F.Cu at (139.6, 132.5)
- added ?: , , F.Cu at (89.7, 132.5)
- added ?: , , F.Cu at (139.6, 107.6)
- added ?: , , F.Cu at (89.7, 107.6)
- added ?: , , F.Cu at (139.6, 82.7)
- added ?: , , F.Cu at (89.7, 82.7)
- added ?: , , F.Cu at (139.6, 57.8)
- added ?: , , F.Cu at (140.8, 117.7)
- added ?: , , F.Cu at (90.9, 67.9)
- added ?: , , F.Cu at (89.7, 56.5)
- added ?: , , F.Cu at (90.9, 56.5)
- added ?: , , F.Cu at (89.7, 57.8)
- added ?: , , F.Cu at (90.9, 117.7)
- added ?: , , F.Cu at (140.8, 92.8)
- added ?: , , F.Cu at (90.9, 92.8)
- added ?: , , F.Cu at (140.8, 67.9)
- added ?: , , F.Cu at (140.8, 131.2)
- added ?: , , F.Cu at (90.9, 131.2)
- added C1: 100n, Capacitors_ThroughHole:C_Rect_L4.6mm_W2.0mm_P2.50mm_MKS02_FKP02, F.Cu at (132.2, 125.7)
- added C1: 100n, Capacitors_ThroughHole:C_Rect_L4.6mm_W2.0mm_P2.50mm_MKS02_FKP02, F.Cu at (82.3, 125.7)
- added C1: 100n, Capacitors_ThroughHole:C_Rect_L4.6mm_W2.0mm_P2.50mm_MKS02_FKP02, F.Cu at (132.2, 100.8)
- added C1: 100n, Capacitors_ThroughHole:C_Rect_L4.6mm_W2.0mm_P2.50mm_MKS02_FKP02, F.Cu at (82.3, 100.8)
- added C1: 100n, Capacitors_ThroughHole:C_Rect_L4.6mm_W2.0mm_P2.50mm_MKS02_FKP02, F.Cu at (132.2, 75.9)
- added C1: 100n, Capacitors_ThroughHole:C_Rect_L4.6mm_W2.0mm_P2.50mm_MKS02_FKP02, F.Cu at (82.3, 75.9)
- added C1: 100n, Capacitors_ThroughHole:C_Rect_L4.6mm_W2.0mm_P2.50mm_MKS02_FKP02, F.Cu at (132.2, 51.1)
- added C1: 100n, Capacitors_ThroughHole:C_Rect_L4.6mm_W2.0mm_P2.50mm_MKS02_FKP02, F.Cu at (82.3, 51.1)
- added C2: 4.7u, Capacitors_ThroughHole:CP_Radial_D4.0mm_P1.50mm, F.Cu at (143.8, 136.3)
- added C2: 4.7u, Capacitors_ThroughHole:CP_Radial_D4.0mm_P1.50mm, F.Cu at (93.9, 136.3)
- added C2: 4.7u, Capacitors_ThroughHole:CP_Radial_D4.0mm_P1.50mm, F.Cu at (143.8, 111.4)
- added C2: 4.7u, Capacitors_ThroughHole:CP_Radial_D4.0mm_P1.50mm, F.Cu at (93.9, 111.4)
- added C2: 4.7u, Capacitors_ThroughHole:CP_Radial_D4.0mm_P1.50mm, F.Cu at (143.8, 86.5)
- added C2: 4.7u, Capacitors_ThroughHole:CP_Radial_D4.0mm_P1.50mm, F.Cu at (93.9, 86.5)
- added C2: 4.7u, Capacitors_ThroughHole:CP_Radial_D4.0mm_P1.50mm, F.Cu at (143.8, 61.6)
- added C3: 100n, Capacitors_ThroughHole:C_Rect_L4.6mm_W2.0mm_P2.50mm_MKS02_FKP02, F.Cu at (164.5, 120.1)
- added C3: 100n, Capacitors_ThroughHole:C_Rect_L4.6mm_W2.0mm_P2.50mm_MKS02_FKP02, F.Cu at (114.6, 120.1)
- added C3: 100n, Capacitors_ThroughHole:C_Rect_L4.6mm_W2.0mm_P2.50mm_MKS02_FKP02, F.Cu at (164.5, 95.2)
- added C3: 100n, Capacitors_ThroughHole:C_Rect_L4.6mm_W2.0mm_P2.50mm_MKS02_FKP02, F.Cu at (114.6, 95.2)
- added C3: 100n, Capacitors_ThroughHole:C_Rect_L4.6mm_W2.0mm_P2.50mm_MKS02_FKP02, F.Cu at (164.5, 70.4)
- added C3: 100n, Capacitors_ThroughHole:C_Rect_L4.6mm_W2.0mm_P2.50mm_MKS02_FKP02, F.Cu at (114.6, 70.4)
- added C3: 100n, Capacitors_ThroughHole:C_Rect_L4.6mm_W2.0mm_P2.50mm_MKS02_FKP02, F.Cu at (164.5, 45.5)
- added C3: 100n, Capacitors_ThroughHole:C_Rect_L4.6mm_W2.0mm_P2.50mm_MKS02_FKP02, F.Cu at (114.6, 45.5)
- added D1: LED, LEDs:LED_D3.0mm, F.Cu at (174.1, 129.2)
- added D1: LED, LEDs:LED_D3.0mm, F.Cu at (124.2, 129.2)
- added D1: LED, LEDs:LED_D3.0mm, F.Cu at (174.1, 104.3)
- added D1: LED, LEDs:LED_D3.0mm, F.Cu at (124.2, 104.3)
- added D1: LED, LEDs:LED_D3.0mm, F.Cu at (174.1, 79.4)
- added D1: LED, LEDs:LED_D3.0mm, F.Cu at (124.2, 79.4)
- added D1: LED, LEDs:LED_D3.0mm, F.Cu at (174.1, 54.5)
- added D1: LED, LEDs:LED_D3.0mm, F.Cu at (124.2, 54.5)
- added G***: LOGO, metalunet:metalunet, B.Cu at (159.1, 127.6)
- added G***: LOGO, metalunet:metalunet-mini, F.Cu at (151.6, 111.8)
- added G***: LOGO, metalunet:metalunet-mini, F.Cu at (101.7, 111.8)
- added G***: LOGO, metalunet:metalunet-mini, F.Cu at (151.6, 86.9)
- added G***: LOGO, metalunet:metalunet-mini, F.Cu at (101.7, 86.9)
- added G***: LOGO, metalunet:metalunet-mini, F.Cu at (151.6, 62.0)
- added G***: LOGO, metalunet:metalunet, B.Cu at (109.2, 53.0)
- added G***: LOGO, metalunet:metalunet-mini, F.Cu at (101.7, 62.0)
- added G***: LOGO, metalunet:metalunet, B.Cu at (109.2, 127.6)
- added G***: LOGO, metalunet:metalunet, B.Cu at (159.1, 102.7)
- added G***: LOGO, metalunet:metalunet, B.Cu at (109.2, 102.7)
- added G***: LOGO, metalunet:metalunet, B.Cu at (159.1, 77.9)
- added G***: LOGO, metalunet:metalunet, B.Cu at (109.2, 77.9)
- added G***: LOGO, metalunet:metalunet, B.Cu at (159.1, 53.0)
- added G***: LOGO, metalunet:metalunet-mini, F.Cu at (151.6, 136.7)
- added G***: LOGO, metalunet:metalunet-mini, F.Cu at (101.7, 136.7)
- added H1: MountingHole, Mounting_Holes:MountingHole_3.2mm_M3, F.Cu at (129.9, 118.2)
- added H1: MountingHole, Mounting_Holes:MountingHole_3.2mm_M3, F.Cu at (80.0, 118.2)
- added H1: MountingHole, Mounting_Holes:MountingHole_3.2mm_M3, F.Cu at (129.9, 93.3)
- added H1: MountingHole, Mounting_Holes:MountingHole_3.2mm_M3, F.Cu at (80.0, 93.3)
- added H1: MountingHole, Mounting_Holes:MountingHole_3.2mm_M3, F.Cu at (129.9, 68.5)
- added H1: MountingHole, Mounting_Holes:MountingHole_3.2mm_M3, F.Cu at (80.0, 68.5)
- added H1: MountingHole, Mounting_Holes:MountingHole_3.2mm_M3, F.Cu at (129.9, 43.6)
- added H2: MountingHole, Mounting_Holes:MountingHole_3.2mm_M3, F.Cu at (172.7, 136.0)
- added H2: MountingHole, Mounting_Holes:MountingHole_3.2mm_M3, F.Cu at (122.8, 136.0)
- added H2: MountingHole, Mounting_Holes:MountingHole_3.2mm_M3, F.Cu at (172.7, 111.1)
- added H2: MountingHole, Mounting_Holes:MountingHole_3.2mm_M3, F.Cu at (122.8, 111.1)
- added H2: MountingHole, Mounting_Holes:MountingHole_3.2mm_M3, F.Cu at (172.7, 86.2)
- added H2: MountingHole, Mounting_Holes:MountingHole_3.2mm_M3, F.Cu at (122.8, 86.2)
- added H2: MountingHole, Mounting_Holes:MountingHole_3.2mm_M3, F.Cu at (172.7, 61.3)
- added J1: Conn_01x03_Female, Connectors_Molex:Molex_KK-6410-03_03x2.54mm_Straight, F.Cu at (130.0, 137.5)
- added J1: Conn_01x03_Female, Connectors_Molex:Molex_KK-6410-03_03x2.54mm_Straight, F.Cu at (80.1, 137.5)
- added J1: Conn_01x03_Female, Connectors_Molex:Molex_KK-6410-03_03x2.54mm_Straight, F.Cu at (130.0, 112.6)
- added J1: Conn_01x03_Female, Connectors_Molex:Molex_KK-6410-03_03x2.54mm_Straight, F.Cu at (80.1, 112.6)
- added J1: Conn_01x03_Female, Connectors_Molex:Molex_KK-6410-03_03x2.54mm_Straight, F.Cu at (130.0, 87.8)
- added J1: Conn_01x03_Female, Connectors_Molex:Molex_KK-6410-03_03x2.54mm_Straight, F.Cu at (80.1, 87.8)
- added J1: Conn_01x03_Female, Connectors_Molex:Molex_KK-6410-03_03x2.54mm_Straight, F.Cu at (130.0, 62.9)
- added J2: ISCP, Pin_Headers:Pin_Header_Straight_1x05_Pitch2.54mm, F.Cu at (134.1, 116.0)
- added J2: ISCP, Pin_Headers:Pin_Header_Straight_1x05_Pitch2.54mm, F.Cu at (84.2, 116.0)
- added J2: ISCP, Pin_Headers:Pin_Header_Straight_1x05_Pitch2.54mm, F.Cu at (134.1, 91.1)
- added J2: ISCP, Pin_Headers:Pin_Header_Straight_1x05_Pitch2.54mm, F.Cu at (84.2, 91.1)
- added J2: ISCP, Pin_Headers:Pin_Header_Straight_1x05_Pitch2.54mm, F.Cu at (134.1, 66.2)
- added J2: ISCP, Pin_Headers:Pin_Header_Straight_1x05_Pitch2.54mm, F.Cu at (84.2, 66.2)
- added J2: ISCP, Pin_Headers:Pin_Header_Straight_1x05_Pitch2.54mm, F.Cu at (134.1, 41.3)
- added J3: Conn_01x02_Female, Terminal_Blocks:TerminalBlock_bornier-2_P5.08mm, F.Cu at (172.0, 123.8)
- added J3: Conn_01x02_Female, Terminal_Blocks:TerminalBlock_bornier-2_P5.08mm, F.Cu at (122.0, 123.8)
- added J3: Conn_01x02_Female, Terminal_Blocks:TerminalBlock_bornier-2_P5.08mm, F.Cu at (172.0, 98.9)
- added J3: Conn_01x02_Female, Terminal_Blocks:TerminalBlock_bornier-2_P5.08mm, F.Cu at (122.0, 98.9)
- added J3: Conn_01x02_Female, Terminal_Blocks:TerminalBlock_bornier-2_P5.08mm, F.Cu at (172.0, 74.0)
- added J3: Conn_01x02_Female, Terminal_Blocks:TerminalBlock_bornier-2_P5.08mm, F.Cu at (122.0, 74.0)
- added J3: Conn_01x02_Female, Terminal_Blocks:TerminalBlock_bornier-2_P5.08mm, F.Cu at (172.0, 49.1)
- added J4: Conn_01x03_Female, Connectors_Molex:Molex_KK-6410-03_03x2.54mm_Straight, F.Cu at (137.9, 137.5)
- added J4: Conn_01x03_Female, Connectors_Molex:Molex_KK-6410-03_03x2.54mm_Straight, F.Cu at (88.0, 137.5)
- added J4: Conn_01x03_Female, Connectors_Molex:Molex_KK-6410-03_03x2.54mm_Straight, F.Cu at (137.9, 112.6)
- added J4: Conn_01x03_Female, Connectors_Molex:Molex_KK-6410-03_03x2.54mm_Straight, F.Cu at (88.0, 112.6)
- added J4: Conn_01x03_Female, Connectors_Molex:Molex_KK-6410-03_03x2.54mm_Straight, F.Cu at (137.9, 87.8)
- added J4: Conn_01x03_Female, Connectors_Molex:Molex_KK-6410-03_03x2.54mm_Straight, F.Cu at (88.0, 87.8)
- added J4: Conn_01x03_Female, Connectors_Molex:Molex_KK-6410-03_03x2.54mm_Straight, F.Cu at (137.9, 62.9)
- added JP1: Config, Connect:GS2, B.Cu at (149.0, 134.4)
- added JP1: Config, Connect:GS2, B.Cu at (99.1, 134.4)
- added JP1: Config, Connect:GS2, B.Cu at (149.0, 109.5)
- added JP1: Config, Connect:GS2, B.Cu at (99.1, 109.5)
- added JP1: Config, Connect:GS2, B.Cu at (149.0, 84.6)
- added JP1: Config, Connect:GS2, B.Cu at (99.1, 84.6)
- added JP1: Config, Connect:GS2, B.Cu at (149.0, 59.7)
- added Q1: IRLB8721PBF, TO_SOT_Packages_SMD:TO-252-2, F.Cu at (152.9, 127.1)
- added Q1: IRLB8721PBF, TO_SOT_Packages_SMD:TO-252-2, F.Cu at (103.0, 127.1)
- added Q1: IRLB8721PBF, TO_SOT_Packages_SMD:TO-252-2, F.Cu at (152.9, 102.2)
- added Q1: IRLB8721PBF, TO_SOT_Packages_SMD:TO-252-2, F.Cu at (103.0, 102.2)
- added Q1: IRLB8721PBF, TO_SOT_Packages_SMD:TO-252-2, F.Cu at (152.9, 77.3)
- added Q1: IRLB8721PBF, TO_SOT_Packages_SMD:TO-252-2, F.Cu at (103.0, 77.3)
- added Q1: IRLB8721PBF, TO_SOT_Packages_SMD:TO-252-2, F.Cu at (152.9, 52.5)
- added Q1: IRLB8721PBF, TO_SOT_Packages_SMD:TO-252-2, F.Cu at (103.0, 52.5)
- added Q2: IRLB8721PBF, TO_SOT_Packages_SMD:TO-252-2, F.Cu at (164.7, 129.9)
- added Q2: IRLB8721PBF, TO_SOT_Packages_SMD:TO-252-2, F.Cu at (114.8, 129.9)
- added Q2: IRLB8721PBF, TO_SOT_Packages_SMD:TO-252-2, F.Cu at (164.7, 105.0)
- added Q2: IRLB8721PBF, TO_SOT_Packages_SMD:TO-252-2, F.Cu at (114.8, 105.0)
- added Q2: IRLB8721PBF, TO_SOT_Packages_SMD:TO-252-2, F.Cu at (164.7, 80.1)
- added Q2: IRLB8721PBF, TO_SOT_Packages_SMD:TO-252-2, F.Cu at (114.8, 80.1)
- added Q2: IRLB8721PBF, TO_SOT_Packages_SMD:TO-252-2, F.Cu at (164.7, 55.2)
- added Q2: IRLB8721PBF, TO_SOT_Packages_SMD:TO-252-2, F.Cu at (114.8, 55.2)
- added R1: 1k, Resistors_ThroughHole:R_Axial_DIN0207_L6.3mm_D2.5mm_P7.62mm_Horizontal, F.Cu at (145.8, 126.2)
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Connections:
- C2 pad 1: +5V -> +3V3
- J1 pad 2: VCC -> +3V3
- J2 pad 2: +5V -> +3V3
- J3 pad 1: Net-(J3-Pad1) -> GNDPWR
- J4 pad 2: VCC -> +3V3
- R1 pad 1: Net-(R1-Pad1) -> GND
- R3 pad 2: /PGC -> Net-(C3-Pad1)
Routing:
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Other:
- board size 77.5 x 99.6 mm -> 99.8 x 99.6 mm
- board text removed: "78L05"
- board text removed: "SOT89"
